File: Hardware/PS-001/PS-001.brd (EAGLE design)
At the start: 39.4 x 39.4 mm, 109 parts, among them J1 10144517-042802LF, J2 10144518-041802LF, J3 10144517-042802LF, J4 10144518-041802LF, J6 2X5_0.05_SWD, Q1 STD15P6F6AG, Q2 DMP3018SFVQ-13, Q3 DMP3018SFVQ-13, U1 ATSAMC21E15A-AUT, U2 MAX16935CAUES/V+, U3 MAX16935CAUES/V+, U4 INA186A2IDCKT, U5 INA2180A4IDGKR, U6 NCV8170AXV330T2G, U7 ATA6561-GAQW-N, U8 LM2902DT, U9 LM2902DT

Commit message: updated sch with atsamC21G - brd needs work
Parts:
- removed C33, C34, C35: 100nF, rcl:C0402
- removed D3: (no value), adafruit:SOD-123
- removed R29: 10k, rcl:R0402
- removed U1: ATSAMC21E15A-AUT, SamacSys_Parts:QFP80P900X900X120-32N
- added C46: 1uF, rcl:C0805
- added C47, C48, C49: 100nF, rcl:C0805
- added C50, C51, C52: 100nF, rcl:C0402
- added D4: (no value), adafruit:SOD-123
- added R32: 10k, rcl:R0402
- added U$60: ATSAMC21G17A-AUT, ATSAM:QFP50P900X900X120-48N
- C32: value 1uF -> 100nF
- moved C32 38.2 mm to (57.4, 27.2), flipped to the bottom, turned to 0 degrees
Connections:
- removed net N$20: D3.A, U1.27
- new net N$29: C46.1, C47.1, U$60.43
- new net N$30: D4.A, U$60.21
- net +3.3V_INT_VMON: now also U$60.14; no longer U1.14
- net +3.5V_IMON: now also C52.1, U$60.11; no longer C33.1, U1.11
- net +3.5V_INT_VMON: now also U$60.4; no longer U1.4
- net +3.5V_VMON: now also U$60.8; no longer U1.6
- net +3V3: now also C48.1, C49.1, U$60.17, U$60.36, U$60.44, U$60.6; no longer U1.29, U1.30, U1.9
- net +5V_IMON: now also C51.1, U$60.12; no longer C34.1, U1.12
- net +5V_INT_VMON: now also U$60.9; no longer U1.7
- net +5V_VMON: now also U$60.10; no longer U1.8
- net +V_BAT_IMON: now also C50.1, U$60.13; no longer C35.1, U1.13
- net +V_BAT_INT_VMON: now also U$60.3; no longer U1.3
- net +V_BAT_VMON: now also U$60.7; no longer U1.5
- net CANRX: now also U$60.34; no longer U1.24
- net CANTX: now also U$60.33; no longer U1.23
- net CAN_STBY: now also U$60.39; no longer U1.25
- net DETECT_A: now also U$60.22; no longer U1.1
- net DETECT_B: now also U$60.23; no longer U1.2
- net DGND: now also C46.2, C47.2, C48.2, C49.2, C50.2, C51.2, C52.2, U$60.18, U$60.35, U$60.42, U$60.5; no longer C33.2, C34.2, C35.2, U1.10, U1.28
- net PGND: now also R32.1; no longer R29.1
- net PGOOD_+3.5V: now also U$60.19; no longer U1.15
- net PGOOD_+5V: now also U$60.20; no longer U1.16
- net P_GOOD: now also D4.C, R32.2; no longer D3.C, R29.2
- net RESET: now also U$60.40; no longer U1.26
- net SWCLK: now also U$60.45; no longer U1.31
- net SWDIO: now also U$60.46; no longer U1.32
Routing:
- net N$20: track 26.2 -> 0.00 mm, vias 4 -> 0
- net DGND: track 25.2 -> 16.0 mm, vias 11 -> 8
- net PGOOD_+5V: track 11.0 -> 5.68 mm
- net DETECT_A: track 23.2 -> 19.3 mm
- net DETECT_B: track 23.8 -> 19.9 mm
- net +3V3: track 32.4 -> 29.1 mm
- net P_GOOD: track 8.09 -> 5.24 mm
- net +V_BAT_IMON: track 32.6 -> 30.8 mm
- net +3.5V_INT_VMON: track 34.2 -> 32.7 mm
- net +3.5V_IMON: track 50.6 -> 49.3 mm
- net CANTX: track 2.55 -> 1.21 mm
- net +5V_IMON: track 57.0 -> 55.8 mm
- net +V_BAT_VMON: track 34.9 -> 33.7 mm
- net SWCLK: track 12.4 -> 11.3 mm
- net RESET: track 4.05 -> 3.00 mm
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
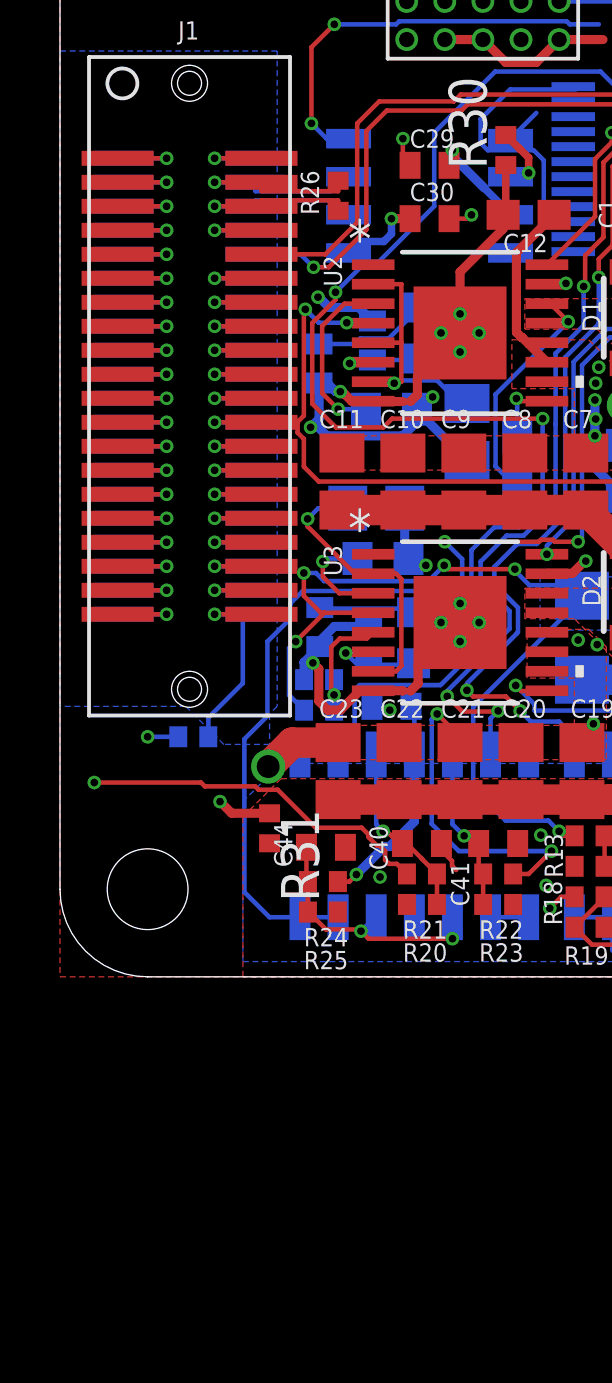
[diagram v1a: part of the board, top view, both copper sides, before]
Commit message: updating voltage rails, should we get rid of
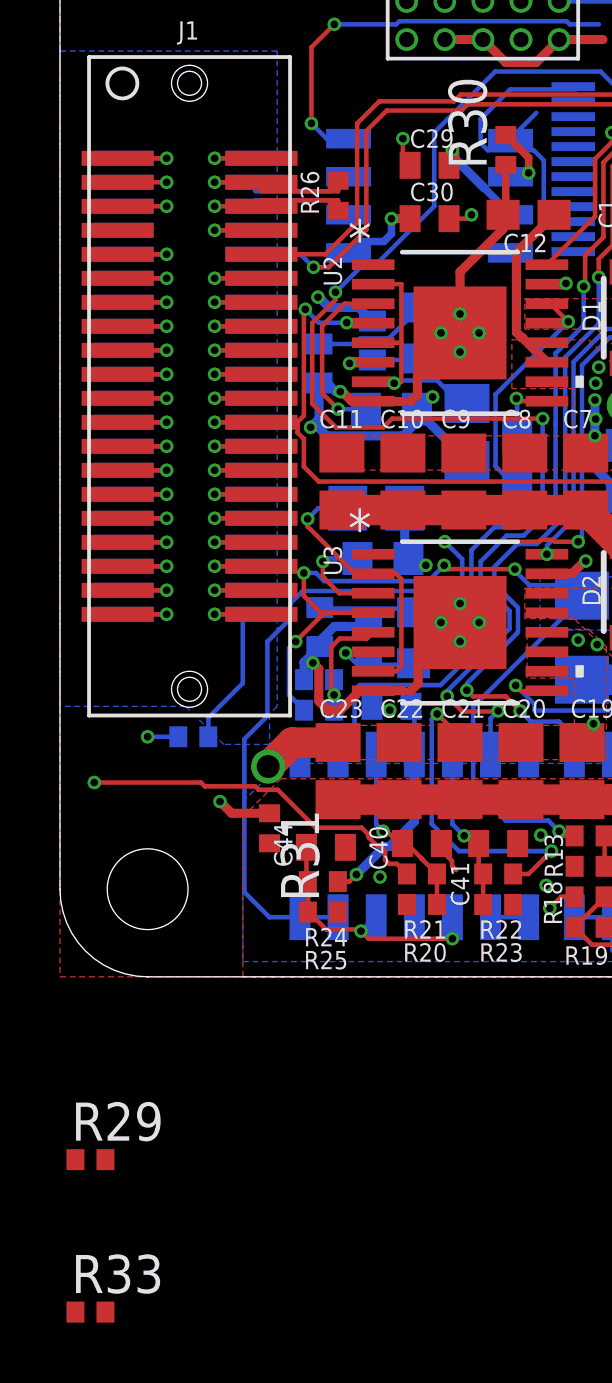
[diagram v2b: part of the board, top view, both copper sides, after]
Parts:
- added R29: 5.6k, rcl:R0402
- added R33: 2.2k, rcl:R0402
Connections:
- net +3.5V_FB renamed +5V_FB
- net CAN_P renamed CAN0_P
- net N$22 renamed VBIAS_U3
- net RFU_3 renamed CAN1_P
- net RFU_5 renamed CAN1_N
- removed net +3.5V_IMON: C52.1, R11.2, U$60.11
- removed net +3.5V_REG: C16.1, C17.1, C18.1, L2.2, R12.2, R27.2, R7.1, SH1.2, U3.4
- removed net RFU_7: J1.7, J2.7
- new net +12V: J3.17, J3.19, J3.21, J3.23, J3.25, J3.27, J3.29, J4.17, J4.19, J4.21, J4.23, J4.25, J4.27, J4.29, Q2.1, Q2.2, Q2.3
- new net +12V_FB: R29.1, R33.2
- new net +12V_IMON: C51.1, R10.2, U$60.12
- new net +12V_REG: C4.1, C5.1, C6.1, L1.2, R16.2, R29.2, R6.1, SH3.2, U2.4
- new net CAN0_N: J2.6
- net +3.5V: no longer C1.1, J3.31, J3.33, J3.35, J3.37, J4.31, J4.33, J4.35, J4.37, Q3.1, Q3.2, Q3.3, U6.1, U6.6
- net +5V: now also C1.1, J3.31, J3.33, J3.35, J3.37, J4.31, J4.33, J4.35, J4.37, Q3.1, Q3.2, Q3.3, U6.1, U6.6; no longer J3.17, J3.19, J3.21, J3.23, J3.25, J3.27, J3.29, J4.17, J4.19, J4.21, J4.23, J4.25, J4.27, J4.29, Q2.1, Q2.2, Q2.3
- net +5V_IMON: now also C52.1, R11.2, U$60.11; no longer C51.1, R10.2, U$60.12
- net +5V_REG: now also C16.1, C17.1, C18.1, L2.2, R12.2, R27.2, R7.1, SH1.2, U3.4; no longer C4.1, C5.1, C6.1, L1.2, R16.2, R6.1, SH3.2, U2.4
- net CAN_N: no longer J2.6
- net GND1: now also R33.1
- net SHIELD: now also J1.7, J2.7
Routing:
- net +12V_IMON: track 0.00 -> 55.8 mm, vias 0 -> 2
- net +3.5V_IMON: track 49.3 -> 0.00 mm, vias 2 -> 0
- net +12V_REG: track 0.00 -> 43.3 mm, vias 0 -> 7
- net +3.5V_REG: track 31.3 -> 0.00 mm, vias 7 -> 0
- net +5V_REG: track 43.3 -> 31.3 mm
- net +5V_IMON: track 55.8 -> 49.3 mm
- net RFU_7: track 3.07 -> 0.00 mm, vias 1 -> 0
- net +3.5V: track 17.6 -> 14.7 mm, vias 6 -> 5
- net +5V: track 40.2 -> 42.7 mm, vias 4 -> 5
- net CAN_N: track 9.52 -> 7.96 mm
- net CAN1_P: track 3.07 -> 1.64 mm
- net CAN1_N: track 3.07 -> 1.64 mm
- added copper zone on layer 1, net +12V_REG
- added copper zone on layer 16, net +12V_REG
- removed copper zone on layer 1, net +3.5V_REG
- removed copper zone on layer 16, net +3.5V_REG

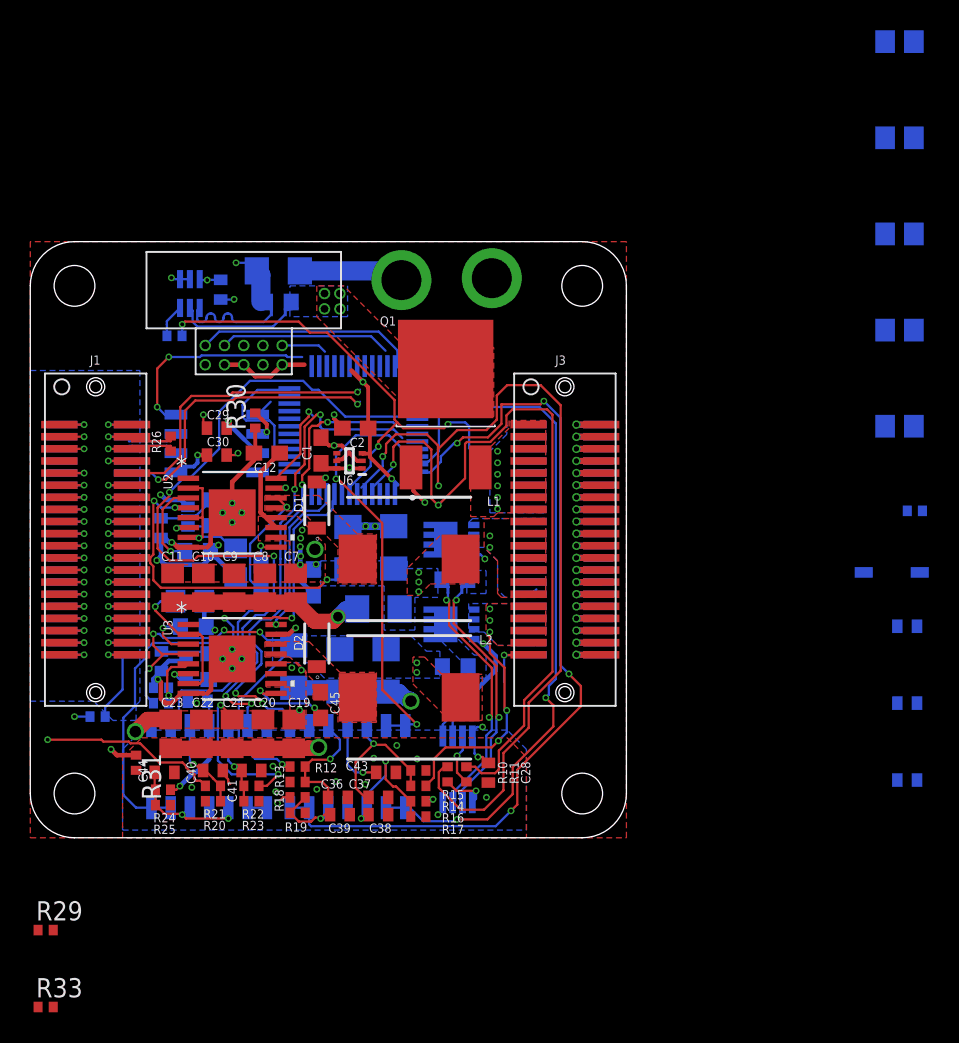
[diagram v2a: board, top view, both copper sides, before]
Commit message: fixed supply ORing
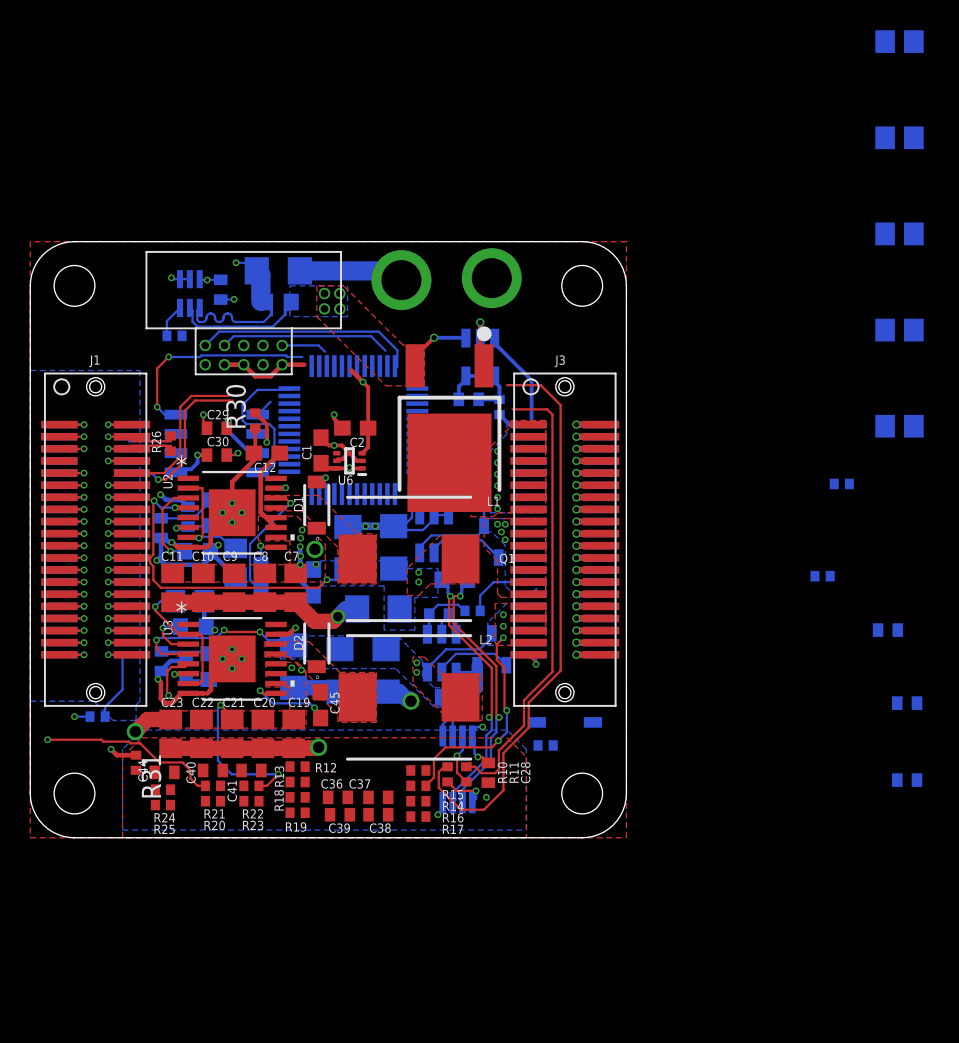
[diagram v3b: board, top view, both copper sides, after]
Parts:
- removed C42, C43: 100nF, rcl:C0402
- removed U8, U9: LM2902DT, SamacSys Managed:SOIC127P600X175-14N
- added C33, C34, C35: 100nF, rcl:C0402
- added IC1, IC2, IC3: LM5050Q1MKX-1_NOPB, SamacSys_Parts:SOT95P280X110-6N
- added R34: 100, rcl:R0402
- Q1: value STD15P6F6AG -> FDD86369-F085; device SamacSys Managed:STD36P4LLF6 -> SamacSys_Parts:DPAK3-CASE-369AS
- Q2, Q3: value DMP3018SFVQ-13 -> DMG6968UQ-7; device SamacSys Managed:DMP3007SFG7 -> SamacSys_Parts:SOT96P240X100-3N
- R27: value 5.6k -> 100
- R28: value 2.2k -> 100
- moved R29 60.3 mm to (53.6, 23.4), flipped to the bottom
- moved R33 58.7 mm to (52.3, 17.3), flipped to the bottom
- moved R32 28.9 mm to (34.0, 6.10)
- moved R27 24.2 mm to (28.4, 22.9), turned to 180 degrees
- moved D4 23.8 mm to (35.3, 7.62), turned to 180 degrees
- moved R28 21.2 mm to (29.2, 15.0)
- moved Q3 3.14 mm to (30.5, 12.4), turned to 90 degrees
- moved Q1 3.06 mm to (27.7, 24.8), turned to 180 degrees
- moved Q2 2.16 mm to (30.0, 19.6), turned to 90 degrees
- moved R7 2.03 mm to (28.1, 9.27)
- moved SH1 2.03 mm to (27.6, 8.56)
- moved SH2 2.03 mm to (28.5, 8.53)
- moved C50 1.30 mm to (56.6, 13.7)
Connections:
- removed net +12V: J3.17, J3.19, J3.21, J3.23, J3.25, J3.27, J3.29, J4.17, J4.19, J4.21, J4.23, J4.25, J4.27, J4.29, Q2.1, Q2.2, Q2.3
- removed net +3.5V: R14.2
- removed net +3.5V_INT_VMON: U$60.4, U9.1, U9.2
- removed net +3.5V_VMON: U$60.8, U9.6, U9.7
- removed net +5V_FB: R27.1, R28.2, U3.5
- removed net N$15: C39.1, R18.1, R19.2, U9.12
- removed net N$23: C37.1, R14.1, R15.2, U9.5
- removed net N$24: C41.1, R22.1, R23.2, U8.5
- removed net N$27: U8.8, U8.9
- new net +12V_INT_VMON: C38.1, R16.1, R17.2, U$60.9
- new net +12V_VMON: C39.1, R18.1, R19.2, U$60.10
- new net N$20: IC2.5, Q2.1
- new net N$22: C34.1, IC2.1, R27.1
- net +12V_FB: now also U2.5
- net +3.3V_INT_VMON: now also C44.1, R24.1, R25.2; no longer U8.13, U8.14
- net +3V3: no longer C42.1, C43.1, U8.4, U9.4
- net +5V: now also IC2.6, IC3.6, J3.17, J3.19, J3.21, J3.23, J3.25, J3.27, J3.29, J4.17, J4.19, J4.21, J4.23, J4.25, J4.27, J4.29, Q2.3, R14.2, R27.2, R28.2; no longer Q3.1, Q3.2
- net +5V_INT_VMON: now also C36.1, R12.1, R13.2, U$60.4; no longer U$60.9, U9.8, U9.9
- net +5V_REG: no longer R27.2
- net +5V_VMON: now also C37.1, R14.1, R15.2, U$60.8; no longer U$60.10, U9.13, U9.14
- net +V_BAT: now also IC1.6, R34.2
- net +V_BAT_INT_VMON: now also C40.1, R20.1, R21.2; no longer U8.1, U8.2
- net +V_BAT_VMON: now also C41.1, R22.1, R23.2; no longer U8.6, U8.7
- net AGND: no longer C42.2, C43.2, U8.11, U9.11
- net GND2: no longer R28.1
- net N$11: now also IC2.4, Q2.2; no longer Q2.5, Q2.6, Q2.7, Q2.8, Q2.9
- net N$12: now also IC3.4, Q3.2; no longer Q3.5, Q3.6, Q3.7, Q3.8, Q3.9
- net N$13: now also IC1.5, Q1.1; no longer C38.1, R16.1, R17.2, U9.10
- net N$14: now also C33.1, IC1.1, R34.1; no longer C36.1, R12.1, R13.2, U9.3
- net N$19: now also IC1.4
- net N$25: now also IC3.5, Q3.1; no longer C44.1, R24.1, R25.2, U8.10, U8.12
- net N$26: now also C35.1, IC3.1, R28.1; no longer C40.1, R20.1, R21.2, U8.3
- net PGND: now also C33.2, C34.2, C35.2, IC1.2, IC1.3, IC2.2, IC2.3, IC3.2, IC3.3; no longer Q1.1, Q2.4, Q3.4
- net VBIAS_U2: no longer U2.5
- net VBIAS_U3: now also U3.5
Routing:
- net +5V_VMON: track 57.1 -> 0.00 mm, vias 4 -> 0
- net +V_BAT_INT_VMON: track 52.1 -> 0.00 mm, vias 2 -> 0
- net +5V_INT_VMON: track 47.9 -> 0.00 mm, vias 2 -> 0
- net +3.3V_INT_VMON: track 35.4 -> 0.00 mm, vias 2 -> 0
- net +V_BAT_VMON: track 33.7 -> 0.00 mm, vias 4 -> 0
- net +3.5V_INT_VMON: track 32.7 -> 0.00 mm, vias 4 -> 0
- net +V_BAT_IMON: track 30.8 -> 0.00 mm, vias 3 -> 0
- net +3.5V_VMON: track 27.6 -> 0.00 mm, vias 2 -> 0
- net +12V_REG: track 43.3 -> 22.7 mm, vias 7 -> 5
- net +5V_IMON: track 49.3 -> 30.1 mm, vias 2 -> 0
- net +12V_IMON: track 55.8 -> 38.2 mm, vias 2 -> 0
- net +5V_REG: track 31.3 -> 14.1 mm, vias 7 -> 5
- net +3V3: track 29.1 -> 14.3 mm, vias 8 -> 5
- net +3.5V: track 14.7 -> 0.00 mm, vias 5 -> 0
- net N$23: track 10.1 -> 0.00 mm, vias 1 -> 0
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- added copper zone on layer 15, net +5V
- removed copper zone on layer 1, net +3.5V
- removed copper zone on layer 15, net +3.5V
- removed copper zone on layer 16, net +3.5V
- removed copper zone on layer 16, net N$11

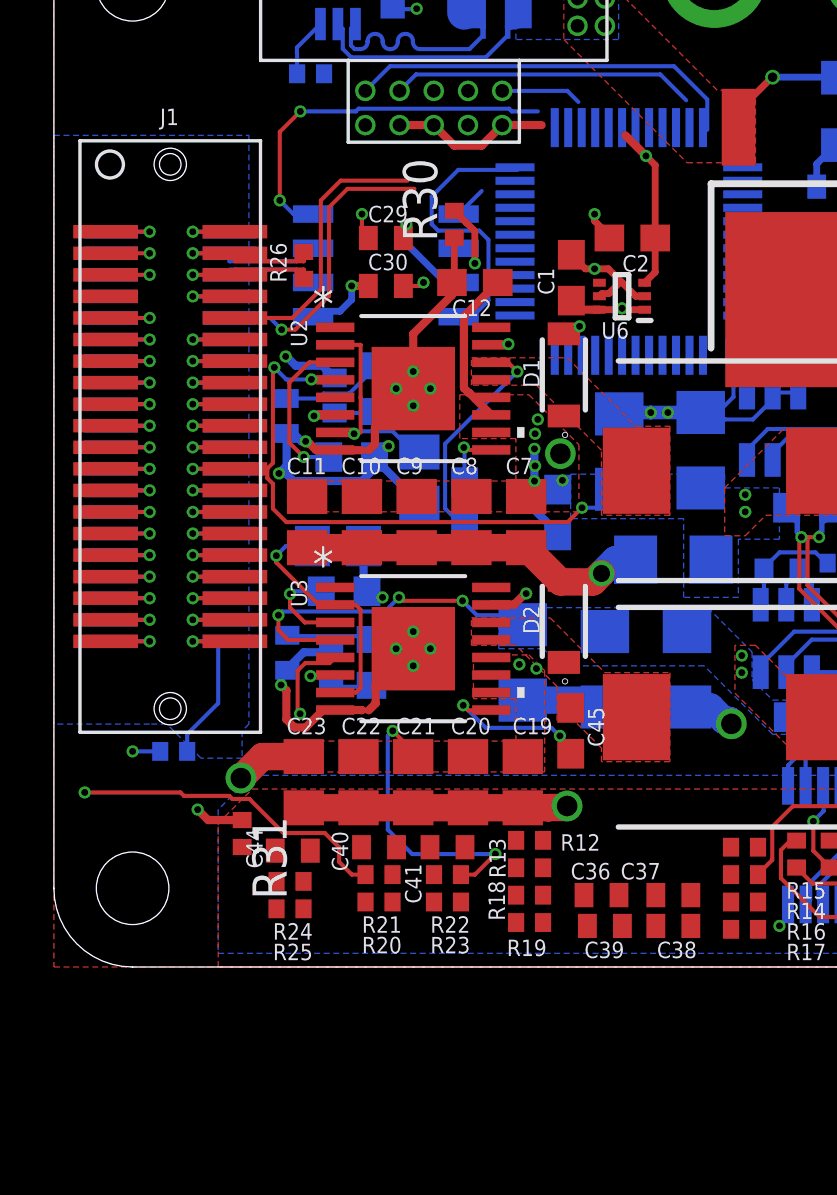
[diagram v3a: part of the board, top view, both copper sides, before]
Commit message: added pullup and swdclk and changed some cap packages
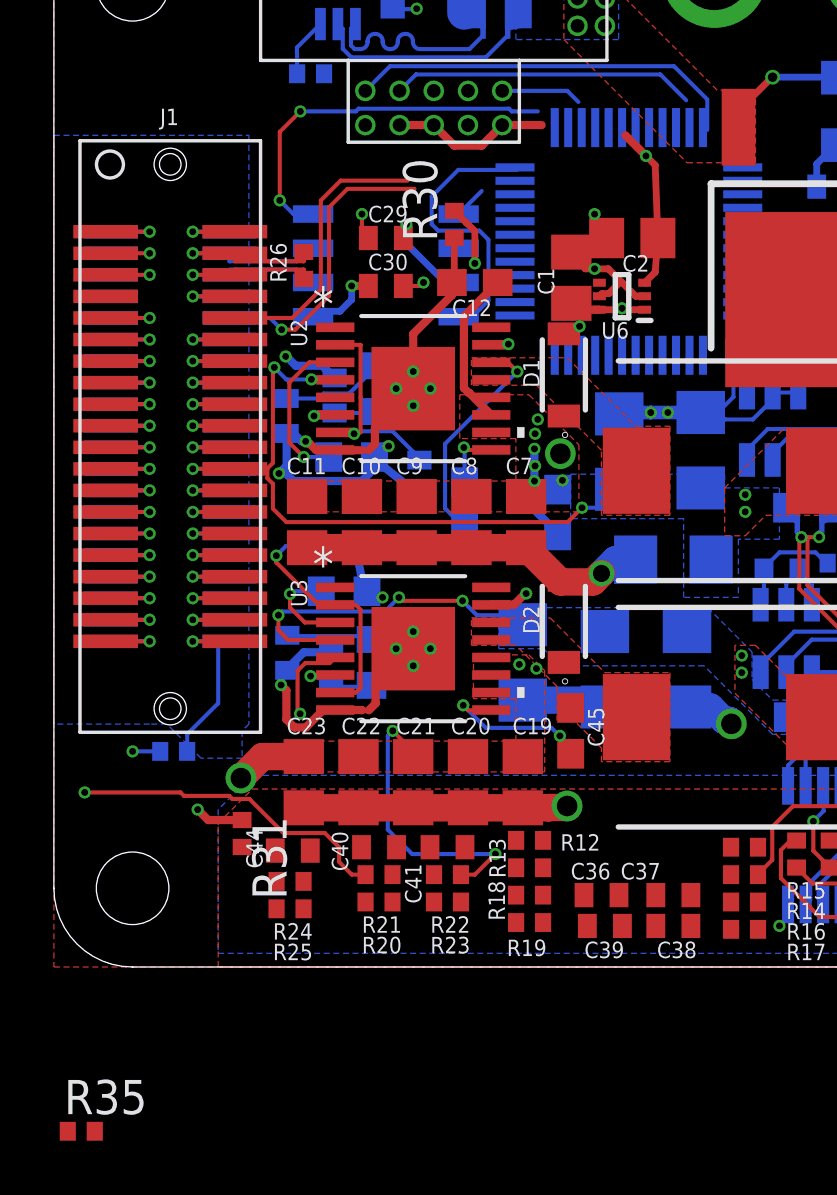
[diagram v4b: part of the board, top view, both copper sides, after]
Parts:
- added R35: 1k, rcl:R0402
- C1, C2: value 1uF -> 10uF; device rcl:C0603 -> rcl:C0805
- C15, C27: device rcl:C0805 -> rcl:C0402
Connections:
- net +3V3: now also R35.2
- net SWCLK: now also R35.1
